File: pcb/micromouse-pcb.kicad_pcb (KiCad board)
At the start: 4 copper layers, 64 parts, among them J1 Conn_01x08, J1_MotorEncoder1 Conn_01x06, J2 Conn_01x08, J2_MotorEncoder1 Conn_01x06, Q1 FQP27P06, Q10 BS170, Q11 TEFT4300, Q12 BS170, Q13 TEFT4300, Q14 BS170, Q15 TEFT4300, Q16 BS170, Q17 TEFT4300, SW3 SW_SPDT, SW4 SW_Push, SW5 SW_Push, U2 AP63205WU, U3 LSM6DSV16XTR

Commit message: connected pins to microcontroller and switched footprint for encoders
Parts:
- added R10: 4.7k, Resistor_SMD:R_0603_1608Metric_Pad0.98x0.95mm_HandSolder, F.Cu at (54.7, 68.3)
- added R11: 4.7k, Resistor_SMD:R_0603_1608Metric_Pad0.98x0.95mm_HandSolder, F.Cu at (54.7, 70.8)
- added R8: 2M, Resistor_SMD:R_0603_1608Metric_Pad0.98x0.95mm_HandSolder, F.Cu at (54.7, 63.3)
- added R9: 1M, Resistor_SMD:R_0603_1608Metric_Pad0.98x0.95mm_HandSolder, F.Cu at (54.7, 65.8)
- added U1: Teensy_4.1, Ratatouii:Teensy4.1_LessHoles, F.Cu at (190.5, 53.2)
- J1_MotorEncoder1, J2_MotorEncoder1: footprint Connector_PinSocket_2.54mm:PinSocket_1x06_P2.54mm_Vertical -> Connector_JST:JST_SH_BM06B-SRSS-TB_1x06-1MP_P1.00mm_Vertical
- moved J2_MotorEncoder1 47.0 mm to (40.0, 57.4)
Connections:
- A2 pad D0: unconnected-(A2-(CRX1)D0-PadD0) -> PWM M2_A
- A2 pad D1: unconnected-(A2-(CTX1)D1-PadD1) -> PWM M2_B
- A2 pad D10: unconnected-(A2-(CS)D10-PadD10) -> ENC_M1_A
- A2 pad D11: unconnected-(A2-(SDO)D11-PadD11) -> ENC_M1_B
- A2 pad D14: unconnected-(A2-A0-PadD14) -> VBAT Sensing
- A2 pad D18: unconnected-(A2-A4-PadD18) -> SDA
- A2 pad D19: unconnected-(A2-A5-PadD19) -> SCL
- A2 pad D2: unconnected-(A2-PadD2) -> PWM M1_A
- A2 pad D20: unconnected-(A2-A6-PadD20) -> Emitter 1
- A2 pad D21: unconnected-(A2-A7-PadD21) -> Emitter 2
- A2 pad D22: unconnected-(A2-A8-PadD22) -> Emitter 3
- A2 pad D23: unconnected-(A2-A9-PadD23) -> Emitter 4
- A2 pad D3: unconnected-(A2-PadD3) -> PWM M1_B
- A2 pad D4: unconnected-(A2-PadD4) -> Receiver 1
- A2 pad D5: unconnected-(A2-PadD5) -> Receiver 2
- A2 pad D6: unconnected-(A2-PadD6) -> Receiver 3
- A2 pad D7: unconnected-(A2-PadD7) -> Receiver 4
- A2 pad D8: unconnected-(A2-PadD8) -> ENC_M2_A
- A2 pad D9: unconnected-(A2-PadD9) -> ENC_M2_B

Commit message: initial layout
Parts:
- removed D1: LED, LED_SMD:LED_1206_3216Metric_Pad1.42x1.75mm_HandSolder
- removed R1, R3: 10k, Resistor_SMD:R_0603_1608Metric_Pad0.98x0.95mm_HandSolder
- removed R4: 1k, Resistor_SMD:R_0603_1608Metric_Pad0.98x0.95mm_HandSolder
- removed R6, R7: 4.7k, Resistor_SMD:R_0603_1608Metric_Pad0.98x0.95mm_HandSolder
- removed SW4, SW5: SW_Push, Button_Switch_SMD:SW_SPST_TL3342
- removed TP3, TP4, TP6: TestPoint, Ratatouii:TestPoint_THTPad_D2.0mm_Drill1.0mm
- removed U1: Teensy_4.1, Ratatouii:Teensy4.1_LessHoles
- added D2: LED, LED_SMD:LED_1206_3216Metric_Pad1.42x1.75mm_HandSolder, F.Cu at (59.2, 85.7)
- added H7: MountingHole, MountingHole:MountingHole_2.2mm_M2, F.Cu at (92.5, 23.5)
- added R12: 1k, Resistor_SMD:R_0603_1608Metric_Pad0.98x0.95mm_HandSolder, F.Cu at (58.4, 88.7)
- added R13: 10k, Resistor_SMD:R_0603_1608Metric_Pad0.98x0.95mm_HandSolder, F.Cu at (58.4, 91.2)
- added SW6: SW_Push, Button_Switch_SMD:SW_SPST_TL3342, F.Cu at (61.0, 80.5)
- added U4: DRV8833PW, Package_SO:TSSOP-16_4.4x5mm_P0.65mm, F.Cu at (40.0, -7.00)
- L1: footprint Inductor_SMD:L_1812_4532Metric_Pad1.30x3.40mm_HandSolder -> Inductor_SMD:L_1008_2520Metric_Pad1.43x2.20mm_HandSolder
- moved U3 146.2 mm to (45.3, 26.2)
- moved L1 121.4 mm to (61.0, 39.0)
- moved Q17 115.1 mm to (71.0, -6.23), turned to 90 degrees
- moved D9 114.8 mm to (65.5, -6.00), turned to 90 degrees
- moved TP1 93.9 mm to (115.0, -4.55)
- moved TP2 93.9 mm to (115.0, -0.50)
- moved TP5 91.7 mm to (115.0, 3.50)
- moved R30 91.7 mm to (49.3, -1.93)
- moved R31 91.7 mm to (49.3, 1.38)
- moved Q16 91.7 mm to (54.2, -3.64)
- moved R29 91.7 mm to (49.3, -5.24)
- moved Q13 90.8 mm to (86.1, 5.57), turned to 90 degrees
- moved D7 88.8 mm to (80.5, 5.77), turned to 90 degrees
- moved D8 85.2 mm to (66.5, 52.8), turned to 90 degrees
- moved Q15 81.6 mm to (72.5, 53.0), turned to 90 degrees
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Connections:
- A2 pad 3.3V: unconnected-(A2-Pad3.3V) -> +3.3V
- J1 pad 2: Net-(J1-Pin_2) -> unconnected-(J1-Pin_2-Pad2)
- J2 pad 1: PWMA_6612 -> unconnected-(J2-Pin_1-Pad1)
- J2 pad 7: PWMB_6612 -> unconnected-(J2-Pin_7-Pad7)
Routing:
- net GND: track 0.00 -> 7.38 mm
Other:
- board outline added: 97.5 x 75 mm
- board text added: "Gyro/Motor Controller"
- board text added: "POWER"

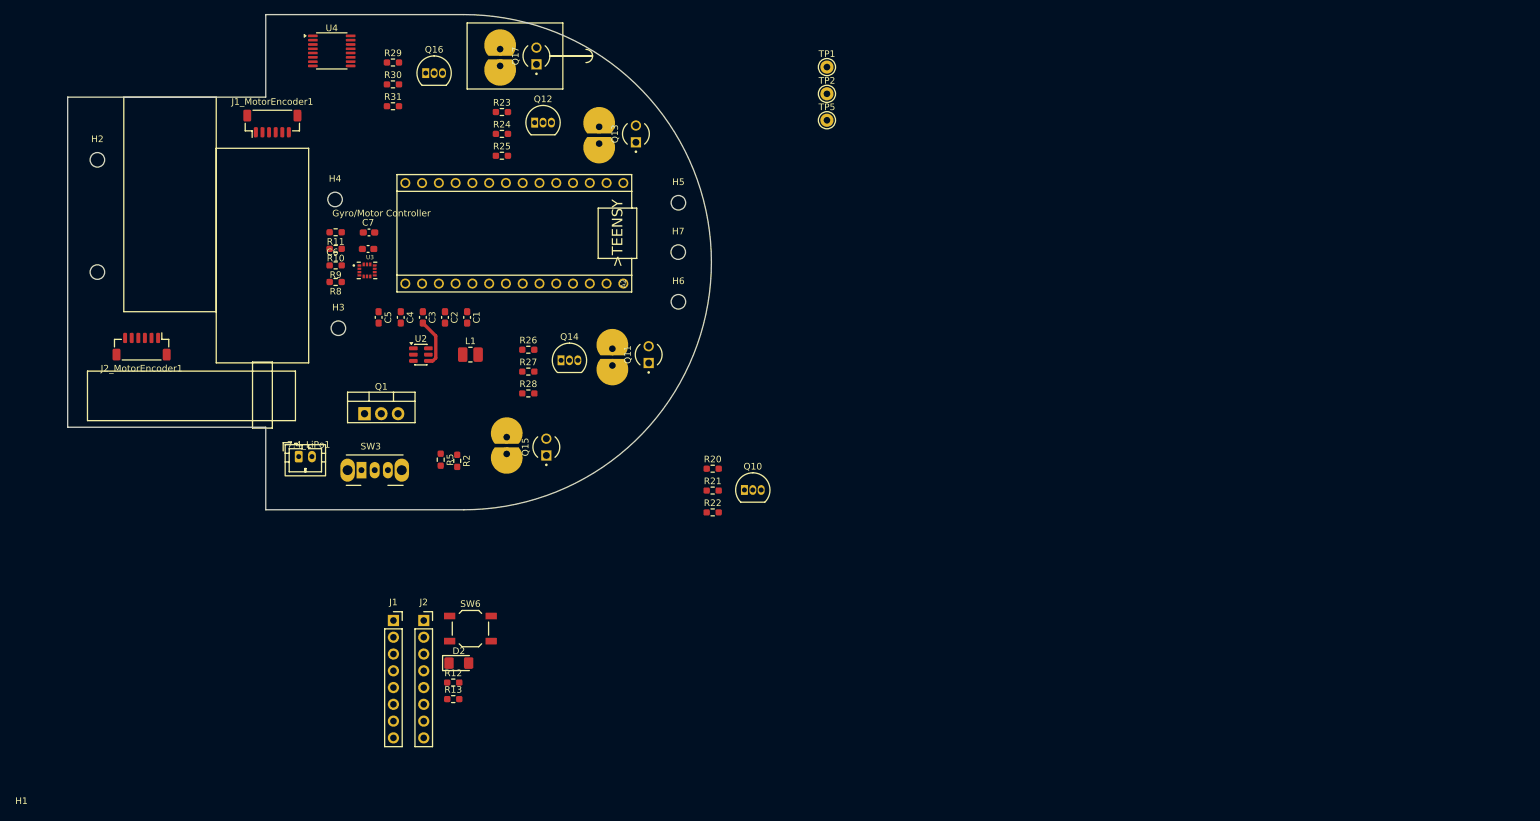
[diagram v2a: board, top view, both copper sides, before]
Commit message: drv8833 schematic; layout component groupingi
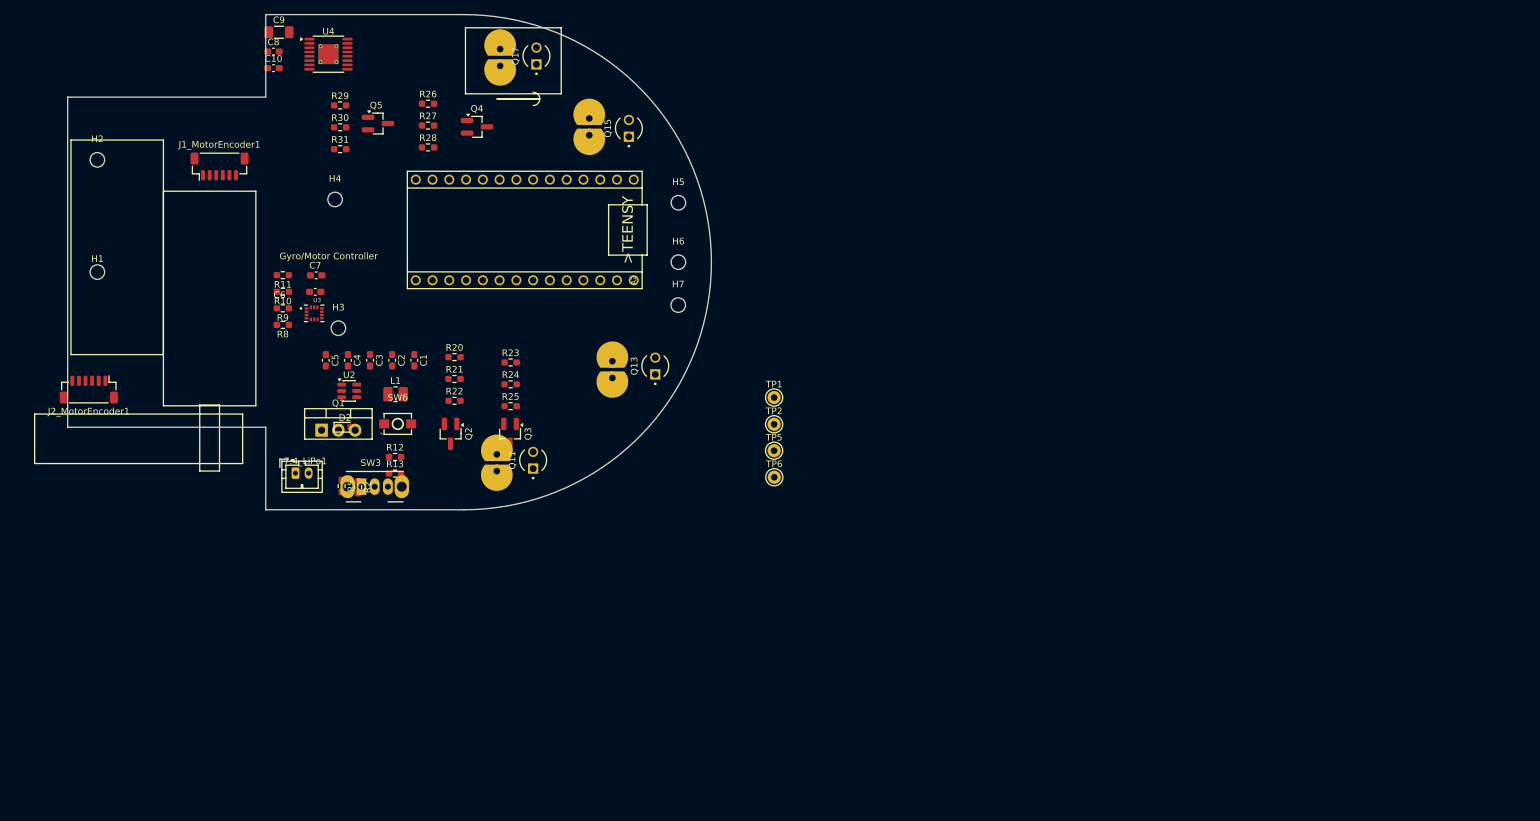
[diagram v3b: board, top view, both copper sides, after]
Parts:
- removed J1, J2: Conn_01x08, Connector_PinSocket_2.54mm:PinSocket_1x08_P2.54mm_Vertical
- removed Q10, Q12, Q14, Q16: BS170, Package_TO_SOT_THT:TO-92_Inline
- added C10: 0.01uF >16V, Capacitor_SMD:C_0603_1608Metric_Pad1.08x0.95mm_HandSolder, F.Cu at (31.2, -4.38)
- added C8: C 2.2uF 6.3V, Capacitor_SMD:C_0603_1608Metric_Pad1.08x0.95mm_HandSolder, F.Cu at (31.2, -6.89)
- added C9: C 47uF >10V, Capacitor_SMD:C_1206_3216Metric_Pad1.33x1.80mm_HandSolder, F.Cu at (32.0, -9.82)
- added Q2: AO3400A, Package_TO_SOT_SMD:SOT-23_Handsoldering, F.Cu at (58.0, 51.0)
- added Q3: AO3400A, Package_TO_SOT_SMD:SOT-23_Handsoldering, F.Cu at (67.0, 51.0)
- added Q4: AO3400A, Package_TO_SOT_SMD:SOT-23_Handsoldering, F.Cu at (62.0, 4.50)
- added Q5: AO3400A, Package_TO_SOT_SMD:SOT-23_Handsoldering, F.Cu at (47.0, 4.00)
- added TP6: TestPoint, Ratatouii:TestPoint_THTPad_D2.0mm_Drill1.0mm, F.Cu at (107.0, 57.6)
- D2: footprint LED_SMD:LED_1206_3216Metric_Pad1.42x1.75mm_HandSolder -> LED_SMD:LED_0603_1608Metric_Pad1.05x0.95mm_HandSolder
- R12: value 1k -> 4.7k
- R21, R24, R27, R30: value 40 -> 36
- SW6: footprint Button_Switch_SMD:SW_SPST_TL3342 -> Ratatouii:SW-SMD_L4.0-W2.9-LS5.0
- U4: footprint Package_SO:TSSOP-16_4.4x5mm_P0.65mm -> Package_SO:TSSOP-16-1EP_4.4x5mm_P0.65mm_EP3x3mm_ThermalVias
- moved TP1 50.7 mm to (107.0, 45.5)
- moved TP2 50.7 mm to (107.0, 49.5)
- moved TP5 50.7 mm to (107.0, 53.5)
- moved D8 49.9 mm to (79.0, 4.50)
- moved Q15 49.9 mm to (85.0, 4.73)
- moved R20 42.6 mm to (58.6, 39.4)
- moved R21 42.6 mm to (58.6, 42.7)
- moved R22 42.6 mm to (58.6, 46.0)
- moved R28 40.2 mm to (54.6, 7.62)
- moved R26 40.2 mm to (54.6, 1.00)
- moved R27 40.2 mm to (54.6, 4.31)
- moved D2 39.7 mm to (42.0, 50.0)
- moved R23 38.0 mm to (67.1, 40.2)
- moved R24 38.0 mm to (67.1, 43.5)
- moved R25 38.0 mm to (67.1, 46.8)
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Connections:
- net ENC_M1_A renamed Encoder L A
- net ENC_M1_B renamed Encoder L B
- net ENC_M2_A renamed Encoder R A
- net ENC_M2_B renamed Encoder R B
- A2 pad D0: PWM M2_A -> Motor R Logic 1
- A2 pad D1: PWM M2_B -> Motor R Logic 2
- A2 pad D12: unconnected-(A2-(SDI)D12-PadD12) -> Gooo button
- A2 pad D2: PWM M1_A -> Motor L Logic 1
- A2 pad D3: PWM M1_B -> Motor L Logic 2
- A2 pad VIN: unconnected-(A2-PadVIN) -> +5V
- D6 pad A: +3.3V -> +5V
- D7 pad A: +3.3V -> +5V
- D8 pad A: +3.3V -> +5V
- D9 pad A: +3.3V -> +5V
- J1_MotorEncoder1 pad 5: POW_M1_A -> Motor L Power 1
- J1_MotorEncoder1 pad 6: POW_M1_B -> Motor L Power 2
- J2_MotorEncoder1 pad 5: POW_M2_A -> Motor R Power 1
- J2_MotorEncoder1 pad 6: POW_M2_B -> Motor R Power 2
- R12 pad 2: unconnected-(R12-Pad2) -> +5V
- R13 pad 2: Net-(R13-Pad2) -> Gooo button
- SW6 pad 1: Net-(R13-Pad2) -> Gooo button
- U4 pad 1: unconnected-(U4-~{SLEEP}-Pad1) -> +3.3V
- U4 pad 10: unconnected-(U4-BIN2-Pad10) -> Motor L Logic 2
- U4 pad 11: unconnected-(U4-VCP-Pad11) -> Net-(U4-VCP)
- U4 pad 12: unconnected-(U4-VM-Pad12) -> 7.4V
- U4 pad 13: unconnected-(U4-GND-Pad13) -> GND
- U4 pad 14: unconnected-(U4-VINT-Pad14) -> Net-(U4-VINT)
- U4 pad 15: unconnected-(U4-AIN2-Pad15) -> Motor R Logic 2
- U4 pad 16: unconnected-(U4-AIN1-Pad16) -> Motor R Logic 1
- U4 pad 2: unconnected-(U4-AOUT1-Pad2) -> Motor R Power 1
- U4 pad 3: unconnected-(U4-AISEN-Pad3) -> GND
- U4 pad 4: unconnected-(U4-AOUT2-Pad4) -> Motor R Power 2
- U4 pad 5: unconnected-(U4-BOUT2-Pad5) -> Motor L Power 2
- U4 pad 6: unconnected-(U4-BISEN-Pad6) -> GND
- U4 pad 7: unconnected-(U4-BOUT1-Pad7) -> Motor L Power 1
- U4 pad 9: unconnected-(U4-BIN1-Pad9) -> Motor L Logic 1
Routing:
- net GND: track 7.38 -> 0.00 mm
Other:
- board text added: "1. IRs, the middle 2 groups need to be rotated 45 degrees (Crossing) 2. Keep in mind spaces for traces when routing 3. Keep the same function groups together (REfer back to schematic if necessary) 4. Decoupling capacitors need to be close to pins 5 Group edge cuts 6 Define positions of things"
